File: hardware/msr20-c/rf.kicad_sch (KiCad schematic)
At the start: 10 parts, among them Q1 2N2907, Q2 2N2222

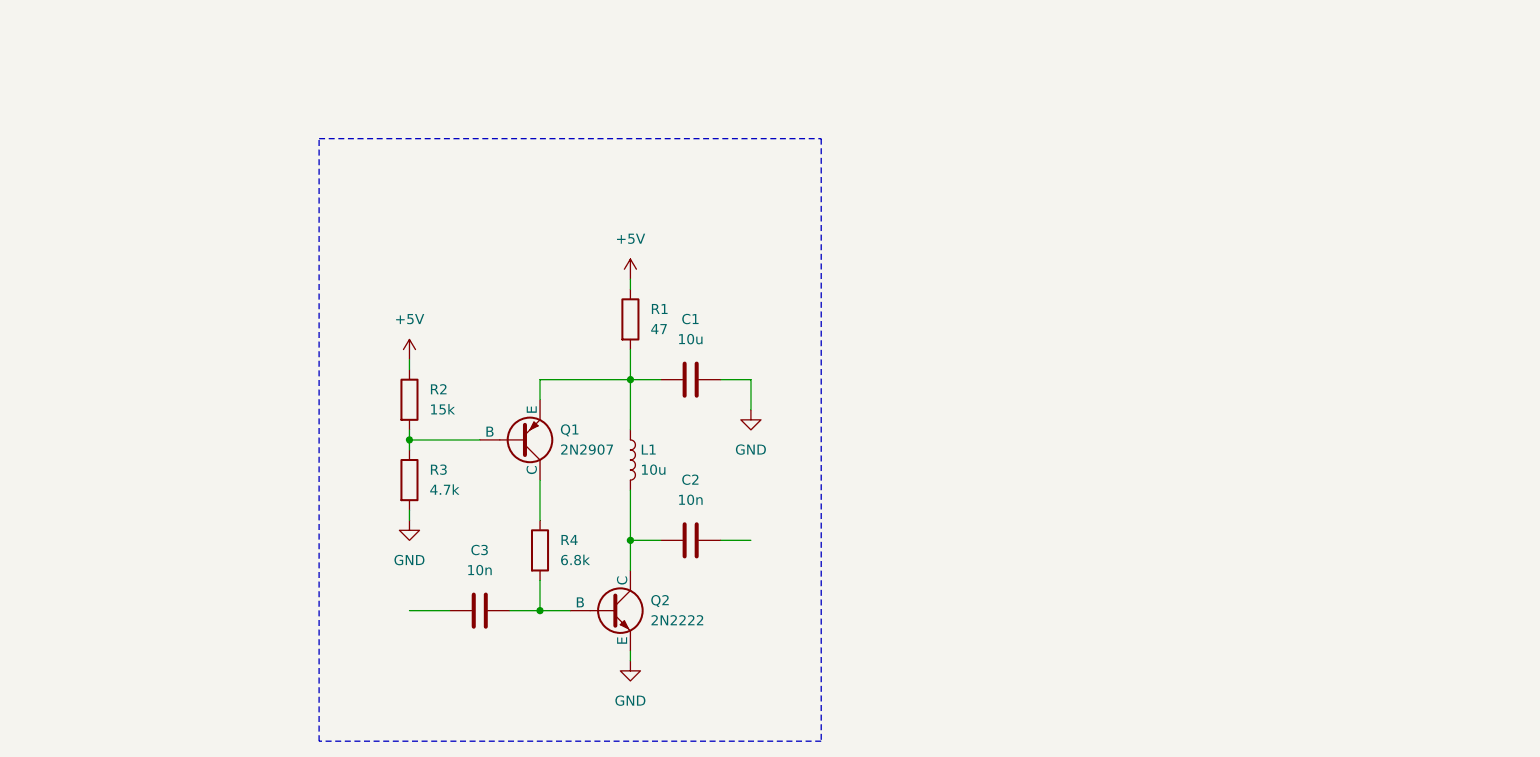
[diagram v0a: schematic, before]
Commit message: draft of rf stage
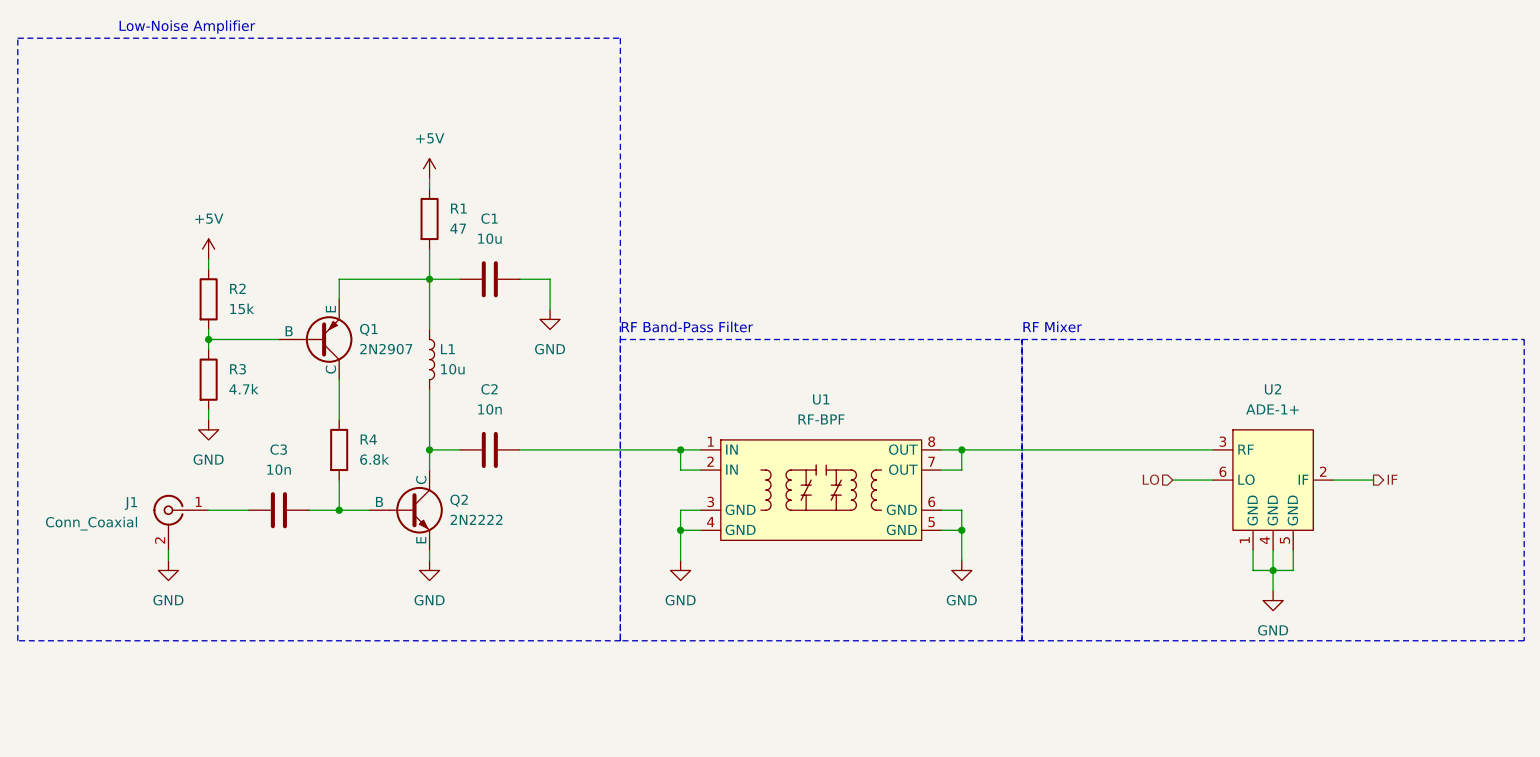
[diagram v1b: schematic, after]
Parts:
- added J1: Conn_Coaxial, symbol Connector:Conn_Coaxial
- added U1: RF-BPF, symbol msr20:RF-BPF
- added U2: ADE-1+, RF_Mini-Circuits:Mini-Circuits_CD542_LandPatternPL-052, symbol msr20:ADE-1+
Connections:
- net GND: now also J1.2 (Ext), U1.3 (GND), U1.4 (GND), U1.5 (GND), U1.6 (GND), U2.1 (GND), U2.4 (GND), U2.5 (GND)
- net at C2.2: now also U1.1 (IN), U1.2 (IN)
- net at C3.1: now also J1.1 (In)
- new net: U1.7 (OUT), U1.8 (OUT), U2.3 (RF)
- new net IF: U2.2 (IF)
- new net LO: U2.6 (LO)
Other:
- note added: "Low-Noise Amplifier"
- note added: "RF Band-Pass Filter"
- note added: "RF Mixer"
- moved on the sheet: C1, C2, C3, L1, Q1, Q2, R1, R2, R3, R4

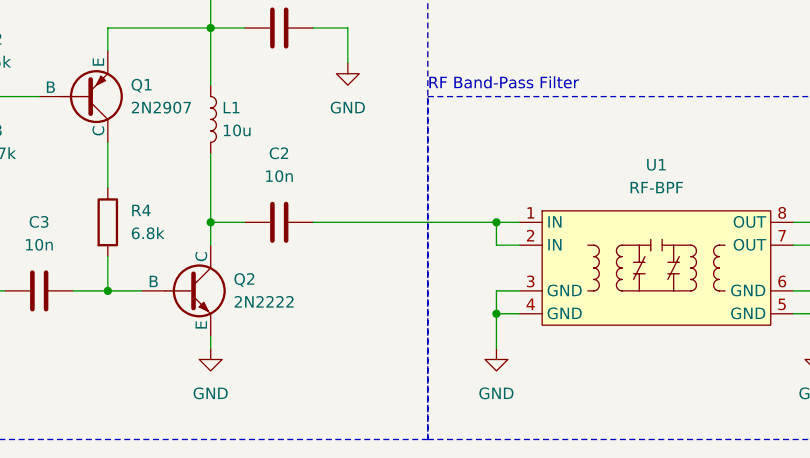
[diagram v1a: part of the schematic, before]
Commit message: add pll to schematic
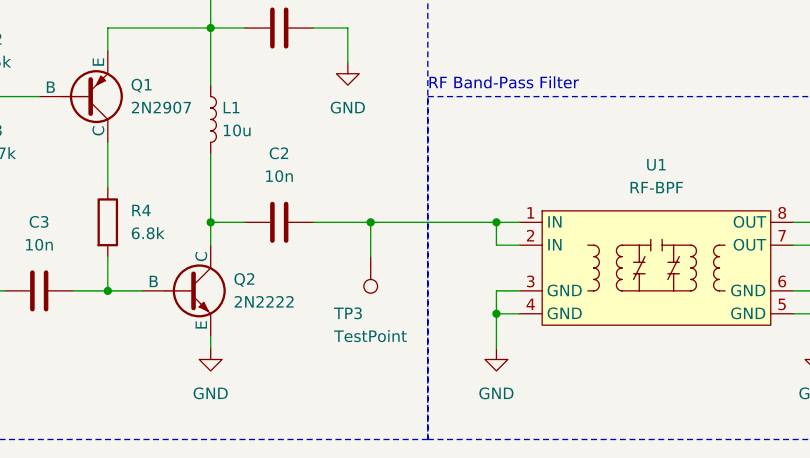
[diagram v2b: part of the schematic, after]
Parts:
- added TP3: TestPoint, TestPoint:TestPoint_Pad_D1.0mm, symbol Connector:TestPoint
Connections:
- net at C2.2, U1.1 (IN), U1.2 (IN): now also TP3.1
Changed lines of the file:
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@@
 		(color 0 0 0 0)
 	)
+	(junction
+		(at 95.25 77.47)
+		(diameter 0)
+		(color 0 0 0 0)
+	)
 	(wire
 		(pts
@@
 	(wire
 		(pts
+			(xy 95.25 77.47) (xy 95.25 81.28)
+		)
+		(stroke
+			(width 0)
+			(type default)
+		)
+	)
+	(wire
+		(pts
+			(xy 95.25 77.47) (xy 109.22 77.47)
+		)
+		(stroke
+			(width 0)
+			(type default)
+		)
+	)
+	(wire
+		(pts
 			(xy 49.53 53.34) (xy 49.53 54.61)
 		)
@@
 	(wire
 		(pts
-			(xy 88.9 77.47) (xy 109.22 77.47)
+			(xy 88.9 77.47) (xy 95.25 77.47)
 		)
 		(stroke
@@
 					(unit 1)
 				)
+			)
+		)
+	)
+	(symbol
+		(lib_id "Connector:TestPoint")
+		(at 95.25 81.28 180)
+		(unit 1)
+		(exclude_from_sim no)
+		(in_bom yes)
+		(on_board yes)
+		(dnp no)
+		(property "Reference" "TP3"
+			(at 91.186 87.63 0)
+			(effects
+				(font
+					(size 1.27 1.27)
+				)
+				(justify right)
+			)
+		)
+		(property "Value" "TestPoint"
+			(at 91.186 90.17 0)
+			(effects
+				(font
+					(size 1.27 1.27)
+				)
+				(justify right)
+			)
+		)
+		(property "Footprint" "TestPoint:TestPoint_Pad_D1.0mm"
+			(at 90.17 81.28 0)
+			(effects
+				(font
+					(size 1.27 1.27)
+				)
+				(hide yes)
+			)
+		)
+		(property "Datasheet" "~"
+			(at 90.17 81.28 0)
+			(effects
+				(font
+					(size 1.27 1.27)
+				)
+				(hide yes)
+			)
+		)
+		(property "Description" "test point"
+			(at 95.25 81.28 0)
+			(effects
+				(font
+					(size 1.27 1.27)
+				)
+				(hide yes)
+			)
+		)
+		(pin "1"
+		)
+		(instances
+			(project "msr20-c"
+				(path "/3d24e86e-b070-4f0e-8c28-04e9dd9d95d1/c9c41028-bd5c-45d5-9f40-d2ea8ca6f8e9"
+					(reference "TP3")
+					(unit 1)
+				)

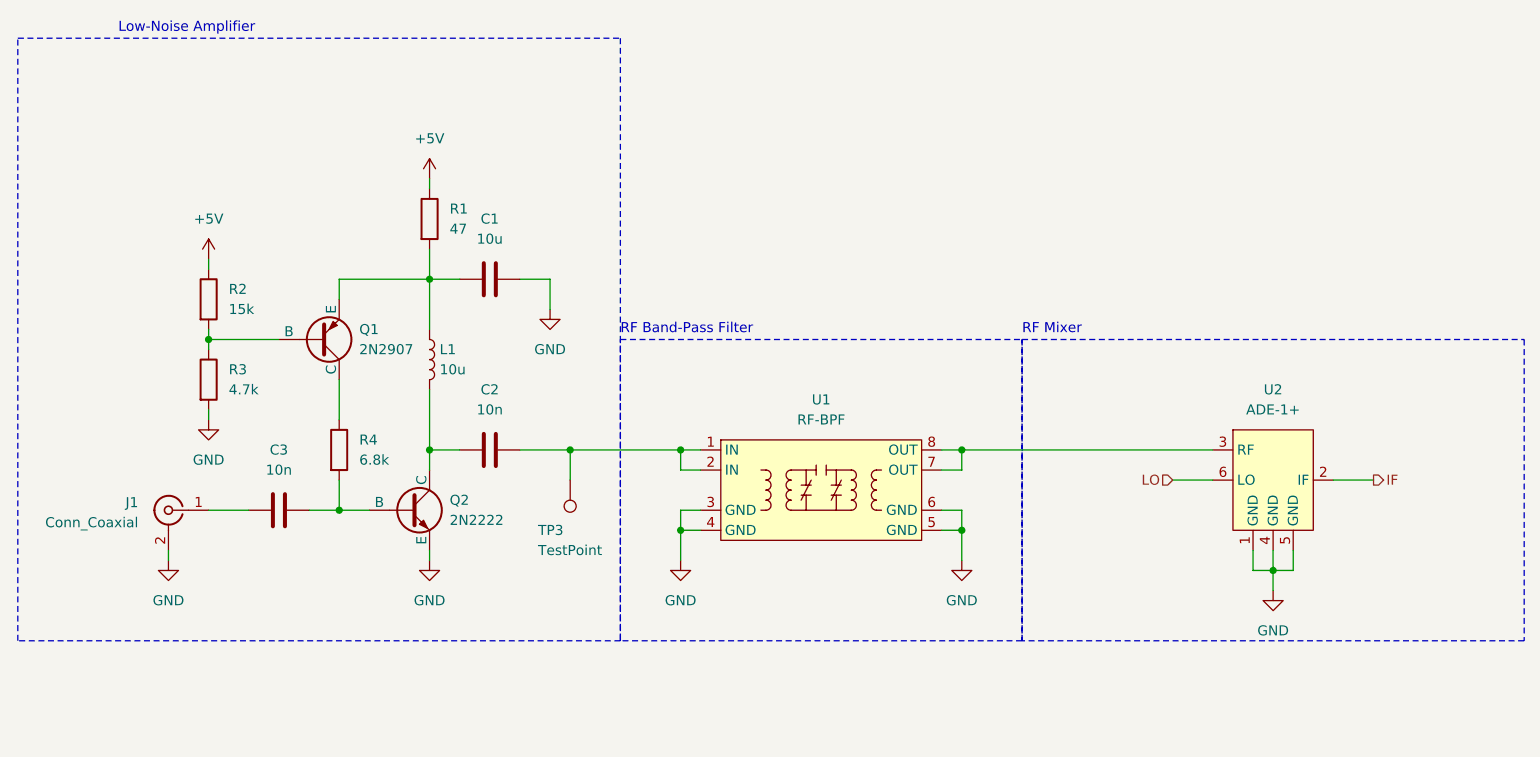
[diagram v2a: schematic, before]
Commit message: add power sheet, assign footprints
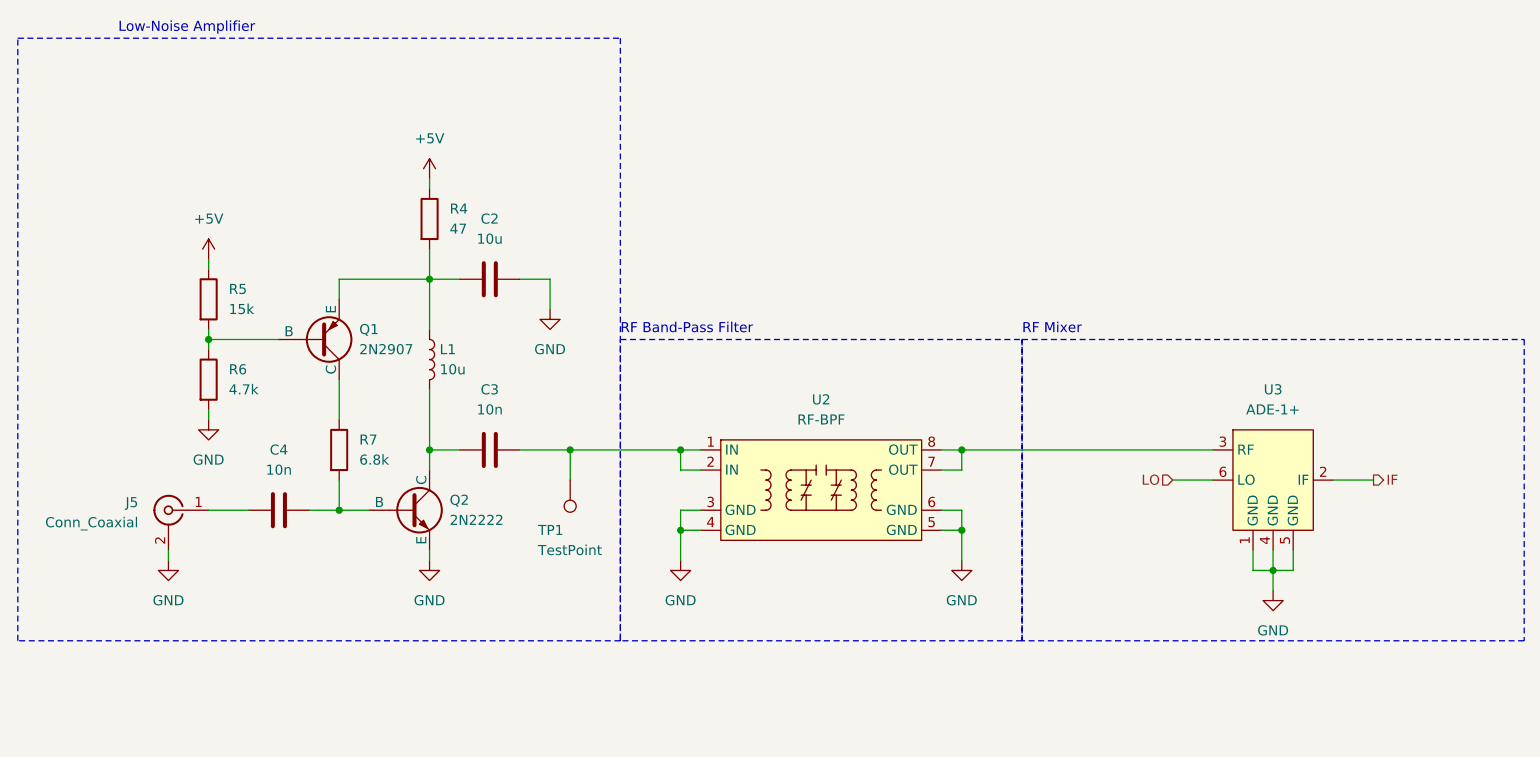
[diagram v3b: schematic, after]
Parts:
- C2: renamed from C1; footprint (none) -> Capacitor_SMD:C_0805_2012Metric
- C3: renamed from C2; footprint (none) -> Capacitor_SMD:C_0805_2012Metric
- C4: renamed from C3; footprint (none) -> Capacitor_SMD:C_0805_2012Metric
- J5: renamed from J1; footprint (none) -> Connector_Coaxial:BNC_Amphenol_031-5539_Vertical
- L1: footprint (none) -> Inductor_SMD:L_0805_2012Metric
- Q1, Q2: footprint (none) -> Package_TO_SOT_THT:TO-92
- R4: renamed from R1; footprint (none) -> Resistor_SMD:R_0805_2012Metric
- R5: renamed from R2; footprint (none) -> Resistor_SMD:R_0805_2012Metric
- R6: renamed from R3; footprint (none) -> Resistor_SMD:R_0805_2012Metric
- R7: renamed from R4; footprint (none) -> Resistor_SMD:R_0805_2012Metric
- U2: renamed from U1; footprint (none) -> msr20:RF-BPF
- renumbered TP3 to TP1, U2 to U3
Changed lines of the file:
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@@
 		(dnp no)
 		(fields_autoplaced yes)
-		(property "Reference" "U2"
+		(property "Reference" "U3"
 			(at 184.15 69.85 0)
 			(effects
@@
 			(project "msr20-c"
 				(path "/3d24e86e-b070-4f0e-8c28-04e9dd9d95d1/c9c41028-bd5c-45d5-9f40-d2ea8ca6f8e9"
-					(reference "U2")
+					(reference "U3")
 					(unit 1)
 				)
@@
 			)
 		)
-		(property "Footprint" ""
+		(property "Footprint" "Inductor_SMD:L_0805_2012Metric"
 			(at 77.47 66.04 0)
 			(effects
@@
 		(dnp no)
 		(fields_autoplaced yes)
-		(property "Reference" "C2"
+		(property "Reference" "C3"
 			(at 85.09 69.85 90)
 			(effects
@@
 			)
 		)
-		(property "Footprint" ""
+		(property "Footprint" "Capacitor_SMD:C_0805_2012Metric"
 			(at 88.9 76.5048 0)
 			(effects
@@
 			(project "msr20-c"
 				(path "/3d24e86e-b070-4f0e-8c28-04e9dd9d95d1/c9c41028-bd5c-45d5-9f40-d2ea8ca6f8e9"
-					(reference "C2")
+					(reference "C3")
 					(unit 1)
 				)
@@
 		(dnp no)
 		(fields_autoplaced yes)
-		(property "Reference" "R2"
+		(property "Reference" "R5"
 			(at 52.07 57.1499 0)
 			(effects
@@
 			)
 		)
-		(property "Footprint" ""
+		(property "Footprint" "Resistor_SMD:R_0805_2012Metric"
 			(at 47.752 58.42 90)
 			(effects
@@
 			(project "msr20-c"
 				(path "/3d24e86e-b070-4f0e-8c28-04e9dd9d95d1/c9c41028-bd5c-45d5-9f40-d2ea8ca6f8e9"
-					(reference "R2")
+					(reference "R5")
 					(unit 1)
 				)
@@
 		(on_board yes)
 		(dnp no)
-		(property "Reference" "J1"
+		(property "Reference" "J5"
 			(at 40.64 84.1131 0)
 			(effects
@@
 			)
 		)
-		(property "Footprint" ""
+		(property "Footprint" "Connector_Coaxial:BNC_Amphenol_031-5539_Vertical"
 			(at 44.45 85.09 0)
 			(effects
@@
 			(project "msr20-c"
 				(path "/3d24e86e-b070-4f0e-8c28-04e9dd9d95d1/c9c41028-bd5c-45d5-9f40-d2ea8ca6f8e9"
-					(reference "J1")
+					(reference "J5")
 					(unit 1)
 				)
@@
 		(dnp no)
 		(fields_autoplaced yes)
-		(property "Reference" "#PWR01"
+		(property "Reference" "#PWR019"
 			(at 77.47 46.99 0)
 			(effects
@@
 			(project "msr20-c"
 				(path "/3d24e86e-b070-4f0e-8c28-04e9dd9d95d1/c9c41028-bd5c-45d5-9f40-d2ea8ca6f8e9"
-					(reference "#PWR01")
+					(reference "#PWR019")
 					(unit 1)
 				)
@@
 		(dnp no)
 		(fields_autoplaced yes)
-		(property "Reference" "#PWR08"
+		(property "Reference" "#PWR023"
 			(at 44.45 97.79 0)
 			(effects
@@
 			(project "msr20-c"
 				(path "/3d24e86e-b070-4f0e-8c28-04e9dd9d95d1/c9c41028-bd5c-45d5-9f40-d2ea8ca6f8e9"
-					(reference "#PWR08")
+					(reference "#PWR023")
 					(unit 1)
 				)
@@
 		(on_board yes)
 		(dnp no)
-		(property "Reference" "TP3"
+		(property "Reference" "TP1"
 			(at 91.186 87.63 0)
 			(effects
@@
 			(project "msr20-c"
 				(path "/3d24e86e-b070-4f0e-8c28-04e9dd9d95d1/c9c41028-bd5c-45d5-9f40-d2ea8ca6f8e9"
-					(reference "TP3")
+					(reference "TP1")
 					(unit 1)
 				)
@@
 		(dnp no)
 		(fields_autoplaced yes)
-		(property "Reference" "#PWR06"
+		(property "Reference" "#PWR025"
 			(at 109.22 97.79 0)
 			(effects
@@
 			(project "msr20-c"
 				(path "/3d24e86e-b070-4f0e-8c28-04e9dd9d95d1/c9c41028-bd5c-45d5-9f40-d2ea8ca6f8e9"
-					(reference "#PWR06")
+					(reference "#PWR025")
 					(unit 1)
 				)
@@
 		(dnp no)
 		(fields_autoplaced yes)
-		(property "Reference" "R1"
+		(property "Reference" "R4"
 			(at 80.01 46.9899 0)
 			(effects
@@
 			)
 		)
-		(property "Footprint" ""
+		(property "Footprint" "Resistor_SMD:R_0805_2012Metric"
 			(at 75.692 48.26 90)
 			(effects
@@
 			(project "msr20-c"
 				(path "/3d24e86e-b070-4f0e-8c28-04e9dd9d95d1/c9c41028-bd5c-45d5-9f40-d2ea8ca6f8e9"
-					(reference "R1")
+					(reference "R4")
 					(unit 1)
 				)
@@
 		(dnp no)
 		(fields_autoplaced yes)
-		(property "Reference" "C3"
+		(property "Reference" "C4"
 			(at 58.42 77.47 90)
 			(effects
@@
 			)
 		)
-		(property "Footprint" ""
+		(property "Footprint" "Capacitor_SMD:C_0805_2012Metric"
 			(at 62.23 84.1248 0)
 			(effects
@@
 			(project "msr20-c"
 				(path "/3d24e86e-b070-4f0e-8c28-04e9dd9d95d1/c9c41028-bd5c-45d5-9f40-d2ea8ca6f8e9"
-					(reference "C3")
+					(reference "C4")
 					(unit 1)
 				)
@@
 		(dnp no)
 		(fields_autoplaced yes)
-		(property "Reference" "R4"
+		(property "Reference" "R7"
 			(at 68.58 76.1999 0)
 			(effects
@@
 			)
 		)
-		(property "Footprint" ""
+		(property "Footprint" "Resistor_SMD:R_0805_2012Metric"
 			(at 64.262 77.47 90)
 			(effects
@@
 			(project "msr20-c"
 				(path "/3d24e86e-b070-4f0e-8c28-04e9dd9d95d1/c9c41028-bd5c-45d5-9f40-d2ea8ca6f8e9"
-					(reference "R4")
+					(reference "R7")
 					(unit 1)
 				)
@@
 		(dnp no)
 		(fields_autoplaced yes)
-		(property "Reference" "#PWR09"
+		(property "Reference" "#PWR027"
 			(at 184.15 101.6 0)
 			(effects
@@
 			(project "msr20-c"
 				(path "/3d24e86e-b070-4f0e-8c28-04e9dd9d95d1/c9c41028-bd5c-45d5-9f40-d2ea8ca6f8e9"
-					(reference "#PWR09")
+					(reference "#PWR027")
 					(unit 1)
 				)
@@
 		(dnp no)
 		(fields_autoplaced yes)
-		(property "Reference" "#PWR03"
+		(property "Reference" "#PWR021"
 			(at 92.71 66.04 0)
 			(effects
@@
 			(project "msr20-c"
 				(path "/3d24e86e-b070-4f0e-8c28-04e9dd9d95d1/c9c41028-bd5c-45d5-9f40-d2ea8ca6f8e9"
-					(reference "#PWR03")
+					(reference "#PWR021")
 					(unit 1)
 				)
@@
 		(dnp no)
 		(fields_autoplaced yes)
-		(property "Reference" "#PWR04"
+		(property "Reference" "#PWR022"
 			(at 49.53 80.01 0)
 			(effects
@@
 			(project "msr20-c"
 				(path "/3d24e86e-b070-4f0e-8c28-04e9dd9d95d1/c9c41028-bd5c-45d5-9f40-d2ea8ca6f8e9"
-					(reference "#PWR04")
+					(reference "#PWR022")
 					(unit 1)
 				)
@@
 		(dnp no)
 		(fields_autoplaced yes)
-		(property "Reference" "R3"
+		(property "Reference" "R6"
 			(at 52.07 67.3099 0)
 			(effects
@@
 			)
 		)
-		(property "Footprint" ""
+		(property "Footprint" "Resistor_SMD:R_0805_2012Metric"
 			(at 47.752 68.58 90)
 			(effects
@@
 			(project "msr20-c"
 				(path "/3d24e86e-b070-4f0e-8c28-04e9dd9d95d1/c9c41028-bd5c-45d5-9f40-d2ea8ca6f8e9"
-					(reference "R3")
+					(reference "R6")
 					(unit 1)
 				)
@@
 		(dnp no)
 		(fields_autoplaced yes)
-		(property "Reference" "C1"
+		(property "Reference" "C2"
 			(at 85.09 48.26 90)
 			(effects
@@
 			)
 		)
-		(property "Footprint" ""
+		(property "Footprint" "Capacitor_SMD:C_0805_2012Metric"
 			(at 88.9 54.9148 0)
 			(effects
@@
 			(project "msr20-c"
 				(path "/3d24e86e-b070-4f0e-8c28-04e9dd9d95d1/c9c41028-bd5c-45d5-9f40-d2ea8ca6f8e9"
-					(reference "C1")
+					(reference "C2")
 					(unit 1)
 				)
@@
 		(dnp no)
 		(fields_autoplaced yes)
-		(property "Reference" "#PWR07"
+		(property "Reference" "#PWR026"
 			(at 144.78 97.79 0)
 			(effects
@@
 			(project "msr20-c"
 				(path "/3d24e86e-b070-4f0e-8c28-04e9dd9d95d1/c9c41028-bd5c-45d5-9f40-d2ea8ca6f8e9"
-					(reference "#PWR07")
+					(reference "#PWR026")
 					(unit 1)
 				)
@@
 		(dnp no)
 		(fields_autoplaced yes)
-		(property "Reference" "U1"
+		(property "Reference" "U2"
 			(at 127 71.12 0)
 			(effects
@@
 			)
 		)
-		(property "Footprint" ""
+		(property "Footprint" "msr20:RF-BPF"
 			(at 127 76.2 0)
 			(effects
@@
 			(project "msr20-c"
 				(path "/3d24e86e-b070-4f0e-8c28-04e9dd9d95d1/c9c41028-bd5c-45d5-9f40-d2ea8ca6f8e9"
-					(reference "U1")
+					(reference "U2")
 					(unit 1)
 				)
@@
 			)
 		)
-		(property "Footprint" ""
+		(property "Footprint" "Package_TO_SOT_THT:TO-92"
 			(at 99.06 63.5 0)
 			(effects
@@
 			)
 		)
-		(property "Footprint" ""
+		(property "Footprint" "Package_TO_SOT_THT:TO-92"
 			(at 138.43 85.09 0)
 			(effects
@@
 		(dnp no)
 		(fields_autoplaced yes)
-		(property "Reference" "#PWR05"
+		(property "Reference" "#PWR024"
 			(at 77.47 97.79 0)
 			(effects
@@
 			(project "msr20-c"
 				(path "/3d24e86e-b070-4f0e-8c28-04e9dd9d95d1/c9c41028-bd5c-45d5-9f40-d2ea8ca6f8e9"
-					(reference "#PWR05")
+					(reference "#PWR024")
 					(unit 1)
 				)
@@
 		(dnp no)
 		(fields_autoplaced yes)
-		(property "Reference" "#PWR02"
+		(property "Reference" "#PWR020"
 			(at 49.53 57.15 0)
 			(effects
@@
 			(project "msr20-c"
 				(path "/3d24e86e-b070-4f0e-8c28-04e9dd9d95d1/c9c41028-bd5c-45d5-9f40-d2ea8ca6f8e9"
-					(reference "#PWR02")
-					(unit 1)
-				)
+					(reference "#PWR020")
+					(unit 1)
+				)
